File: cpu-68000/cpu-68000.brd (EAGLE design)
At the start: 149.9 x 99.7 mm, 101 parts, among them IC201 AS6C4008, IC202 AS6C4008, IC203 39SF040, IC204 39SF040, IC301 XR68C681, IC302 DS1244Y, IC303 MAX232, IC401 GAL22V10, IC402 GAL22V10, IC403 74HC14D, IC404 LM3724, IC405 74HC175D, J201 POWER_JACK, Q301 3.6864 MHz

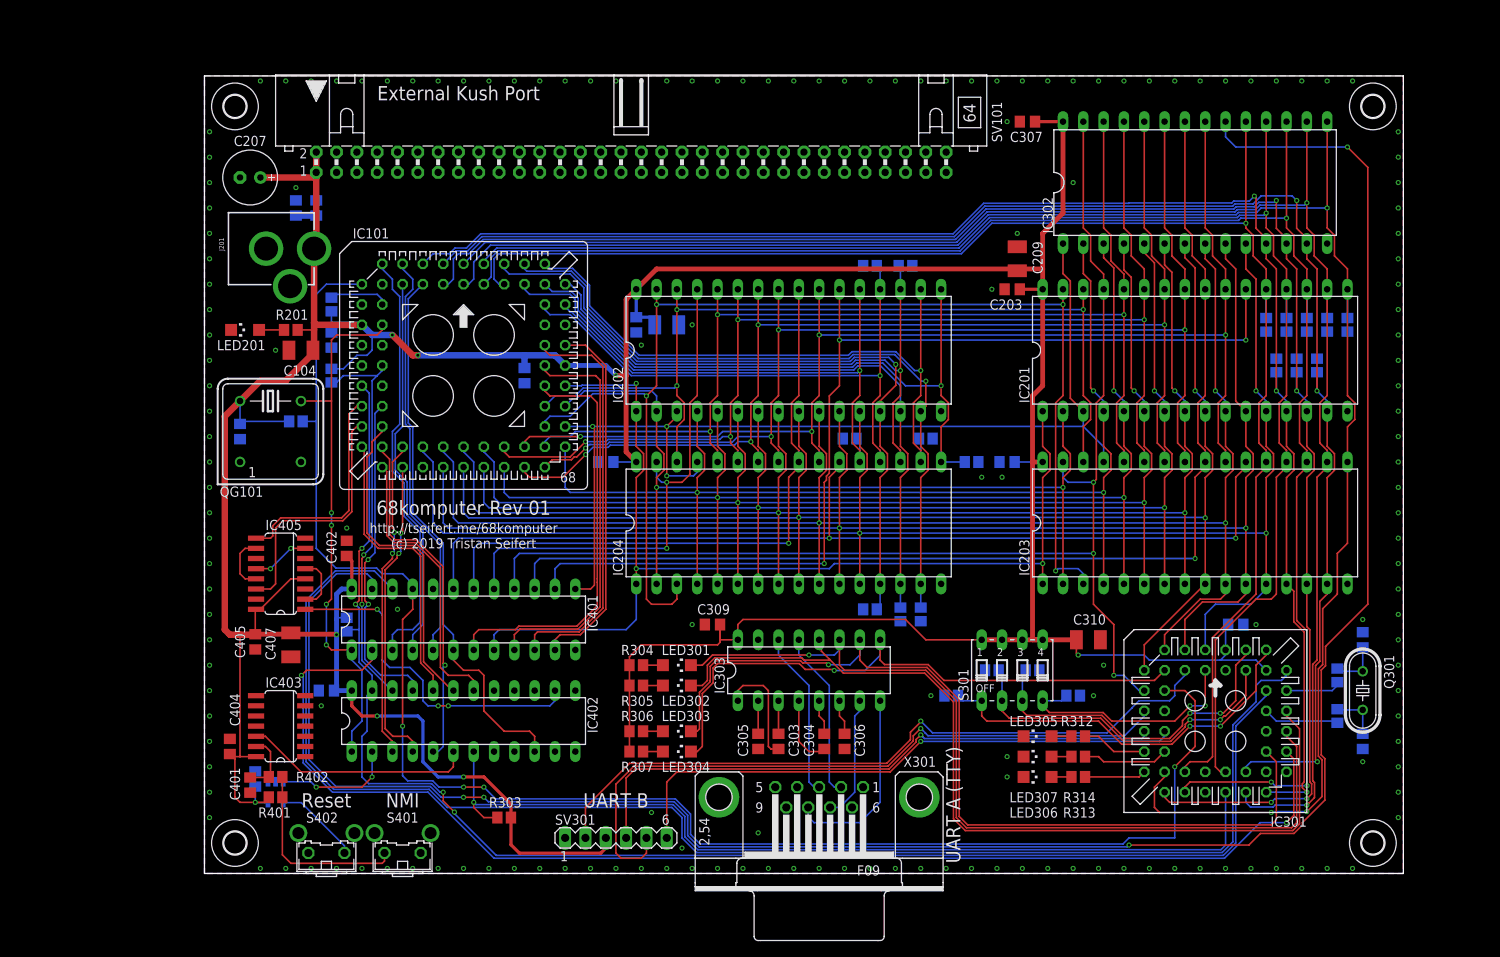
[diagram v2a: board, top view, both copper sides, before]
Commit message: Finished routing expansion connector for 68000 board
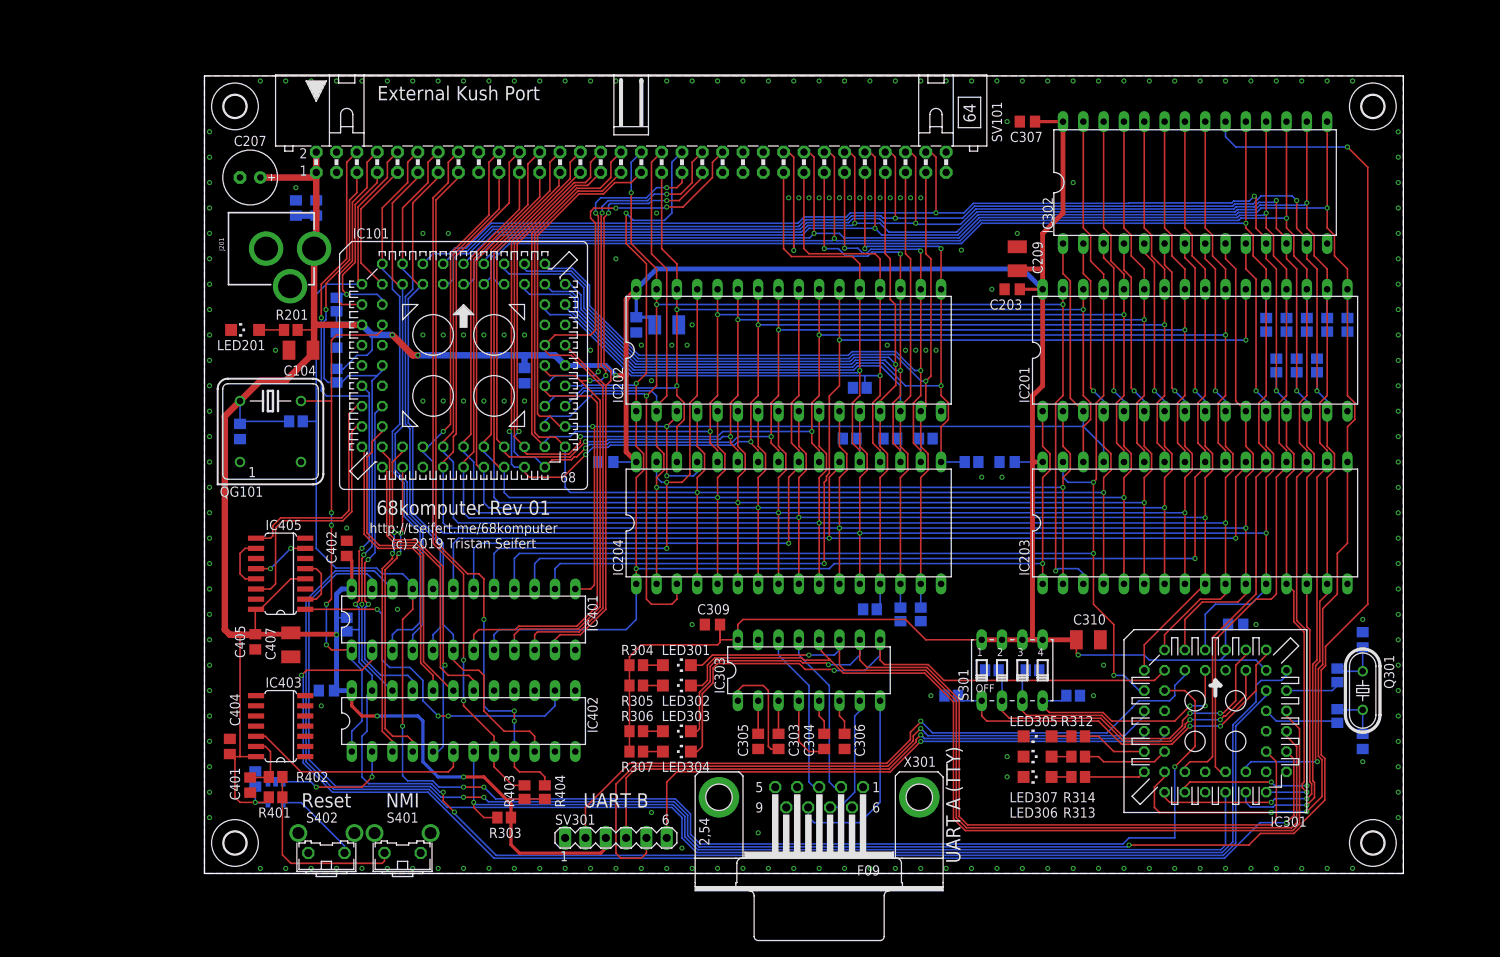
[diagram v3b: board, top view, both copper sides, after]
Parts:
- removed R6, R7: 10k, rcl:R2012
- added R118, R119, R403, R404: 10k, rcl:R2012
- moved C102 0.64 mm to (16.5, 66.7)
- moved R103 0.64 mm to (16.5, 62.2)
- moved R104 0.64 mm to (16.5, 71.1)
- renumbered R1 to R113, R2 to R114, R3 to R115, R4 to R116, R5 to R117, R8 to R120
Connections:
- net !AS: now also SV101.13
- net !BG: now also SV101.9
- net !BGACK: now also SV101.8
- net !BR: now also SV101.7
- net !DTACK: now also SV101.10
- net !EXTI_A: now also R403.1, SV101.16
- net !EXTI_B: now also R404.1, SV101.15
- net !HALT: now also SV101.5
- net !LDS: now also SV101.11
- net !RESET: now also SV101.6
- net !UDS: now also SV101.14
- net +5V: now also R403.2, R404.2
- net A1: now also SV101.20
- net A10: now also SV101.27
- net A11: now also SV101.30
- net A12: now also SV101.29
- net A13: now also SV101.31
- net A14: now also SV101.32
- net A15: now also SV101.33
- net A16: now also SV101.34
- net A17: now also SV101.36
- net A18: now also SV101.35
- net A19: now also SV101.38
- net A2: now also SV101.22
- net A20: now also SV101.37
- net A21: now also SV101.40
- net A22: now also SV101.39
- net A23: now also SV101.42
- net A3: now also SV101.19
- net A4: now also SV101.24
- net A5: now also SV101.21
- net A6: now also SV101.23
- net A7: now also SV101.26
- net A8: now also SV101.25
- net A9: now also SV101.28
- net D0: now also SV101.62
- net D1: now also SV101.60
- net D10: now also SV101.61
- net D11: now also SV101.55
- net D12: now also SV101.53
- net D13: now also R118.2, SV101.51; no longer R6.2
- net D14: now also R119.2, SV101.49; no longer R7.2
- net D15: now also SV101.47
- net D2: now also SV101.58
- net D3: now also SV101.56
- net D4: now also SV101.54
- net D5: now also SV101.52
- net D6: now also SV101.50
- net D7: now also SV101.48
- net D8: now also SV101.57
- net D9: now also SV101.59
- net GND: now also R118.1, R119.1, SV101.17, SV101.18, SV101.45, SV101.46, X301.G1, X301.G2; no longer R6.1, R7.1
- net R/!W!: now also SV101.12
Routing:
- net !EXTI_B: track 0.00 -> 87.6 mm, vias 0 -> 3
- net !EXTI_A: track 0.00 -> 86.1 mm, vias 0 -> 2
- net A12: track 147.4 -> 192.5 mm, vias 4 -> 5
- net A11: track 154.6 -> 198.4 mm
- net A14: track 139.3 -> 183.2 mm
- net A13: track 139.4 -> 182.7 mm
- net A4: track 179.4 -> 222.7 mm
- net A2: track 188.3 -> 231.6 mm
- net A15: track 130.6 -> 173.2 mm
- net A10: track 148.5 -> 190.6 mm, vias 4 -> 5
- net A20: track 52.0 -> 93.8 mm, vias 0 -> 3
- net A9: track 147.7 -> 189.3 mm
- net A23: track 50.8 -> 92.1 mm, vias 0 -> 2
- net A8: track 147.6 -> 188.8 mm
- net A1: track 195.4 -> 236.6 mm, vias 3 -> 4
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
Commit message: Enlarged 68000 board to 100x160mm (Eurocard size) Moved high/low words sections to accomodate ZIF sockets better
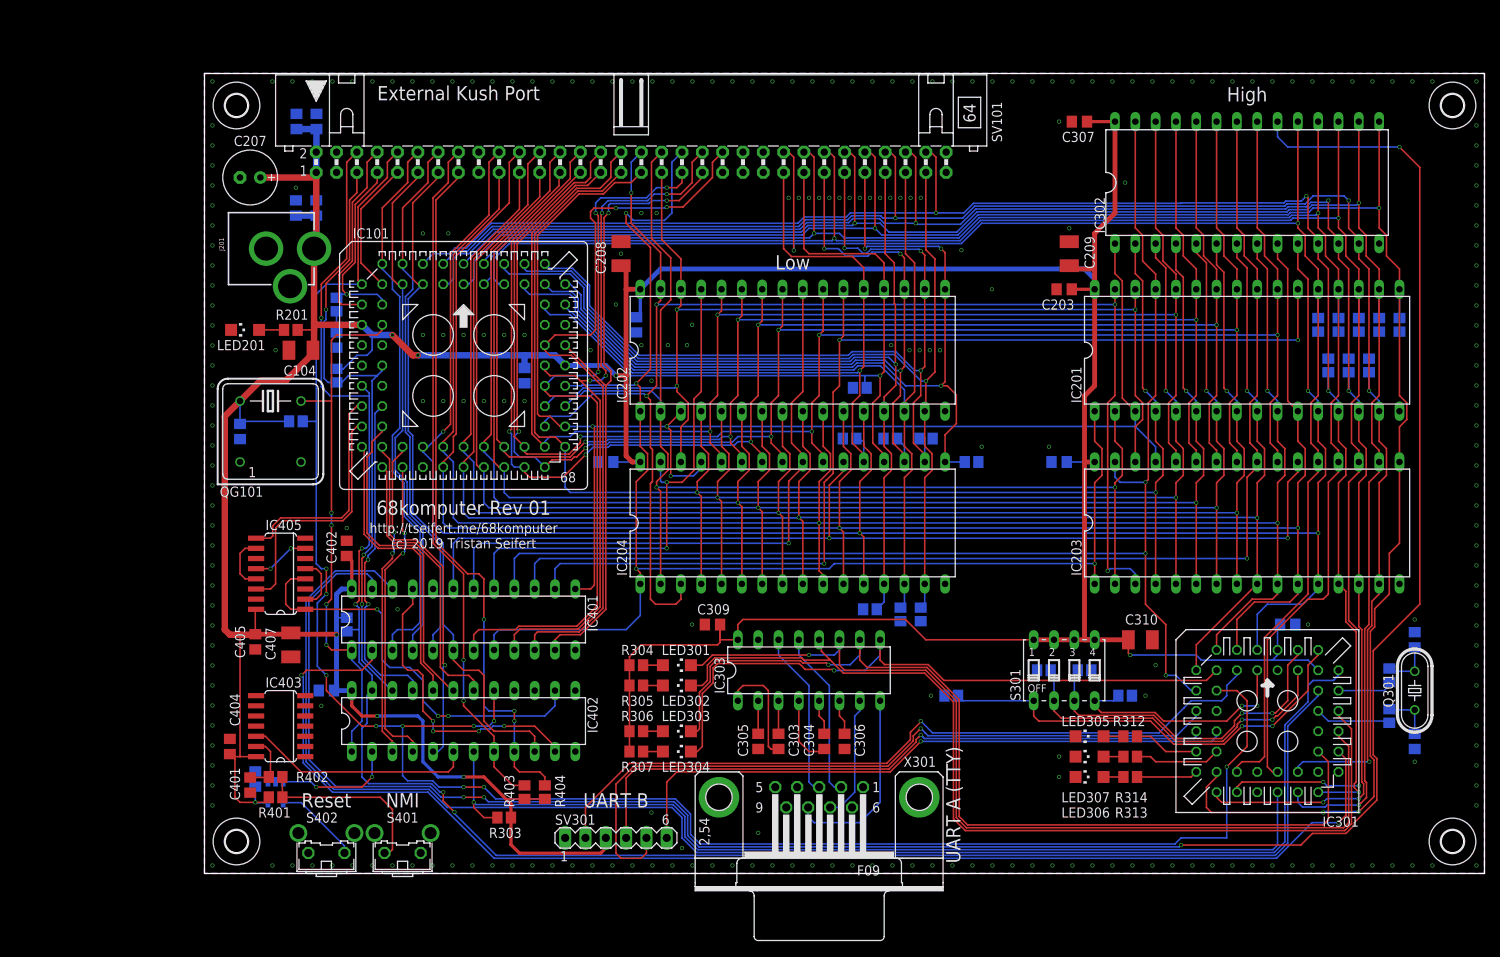
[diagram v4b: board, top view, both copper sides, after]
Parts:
- added C1: 1µF, rcl:C0805
- added C105: 100nF, rcl:C0805
- moved C208 10.6 mm to (52.1, 77.5), flipped to the top, turned to 90 degrees
- moved H104 9.95 mm to (156.0, 4.00)
- moved H103 9.95 mm to (156.0, 96.0)
- moved C209 6.53 mm to (108.1, 77.5)
- moved IC301 6.50 mm to (132.9, 19.1)
- moved C203 6.50 mm to (107.5, 73.0)
- moved C206 6.50 mm to (106.8, 51.4)
- moved C301 6.50 mm to (151.3, 16.5)
- moved C302 6.50 mm to (151.3, 29.2)
- moved C307 6.50 mm to (109.4, 94.0)
- moved C308 6.50 mm to (135.4, 31.1)
- moved C310 6.50 mm to (117.0, 29.2)
- moved LED305 6.50 mm to (110.6, 17.1)
- moved LED306 6.50 mm to (110.6, 12.1)
- moved LED307 6.50 mm to (110.6, 14.6)
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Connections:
- removed net N$22: IC402.11
- removed net N$23: IC402.13
- new net !ADDR_GOOD: IC401.21, IC402.11
- net !BERR_TIMER_CLR: now also IC405.4
- net !DTACK: now also IC402.17; no longer IC401.21
- net +5V: now also C1.1, C105.1; no longer IC405.4
- net GND: now also C1.2, C105.2, SV101.41, SV101.43, SV101.44
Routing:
- net !ADDR_GOOD: track 0.00 -> 37.8 mm, vias 0 -> 4
- net !DTACK: track 221.2 -> 242.0 mm, vias 4 -> 10
- net +5V: track 556.8 -> 570.5 mm
- net !BERR_TIMER_CLR: track 44.0 -> 51.9 mm
- net A19: track 170.7 -> 178.4 mm
- net A16: track 170.9 -> 178.2 mm
- net A17: track 144.1 -> 151.4 mm
- net A18: track 128.5 -> 135.6 mm
- net A2: track 231.6 -> 238.5 mm
- net A9: track 189.3 -> 196.2 mm
- net A5: track 201.2 -> 208.1 mm
- net A10: track 190.6 -> 197.5 mm
- net A8: track 188.8 -> 195.7 mm
- net A7: track 195.9 -> 202.8 mm
- net A6: track 197.4 -> 204.3 mm
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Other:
- board size 149.9 x 99.7 mm -> 160 x 100 mm
- board text added: "High"
- board text added: "Low"

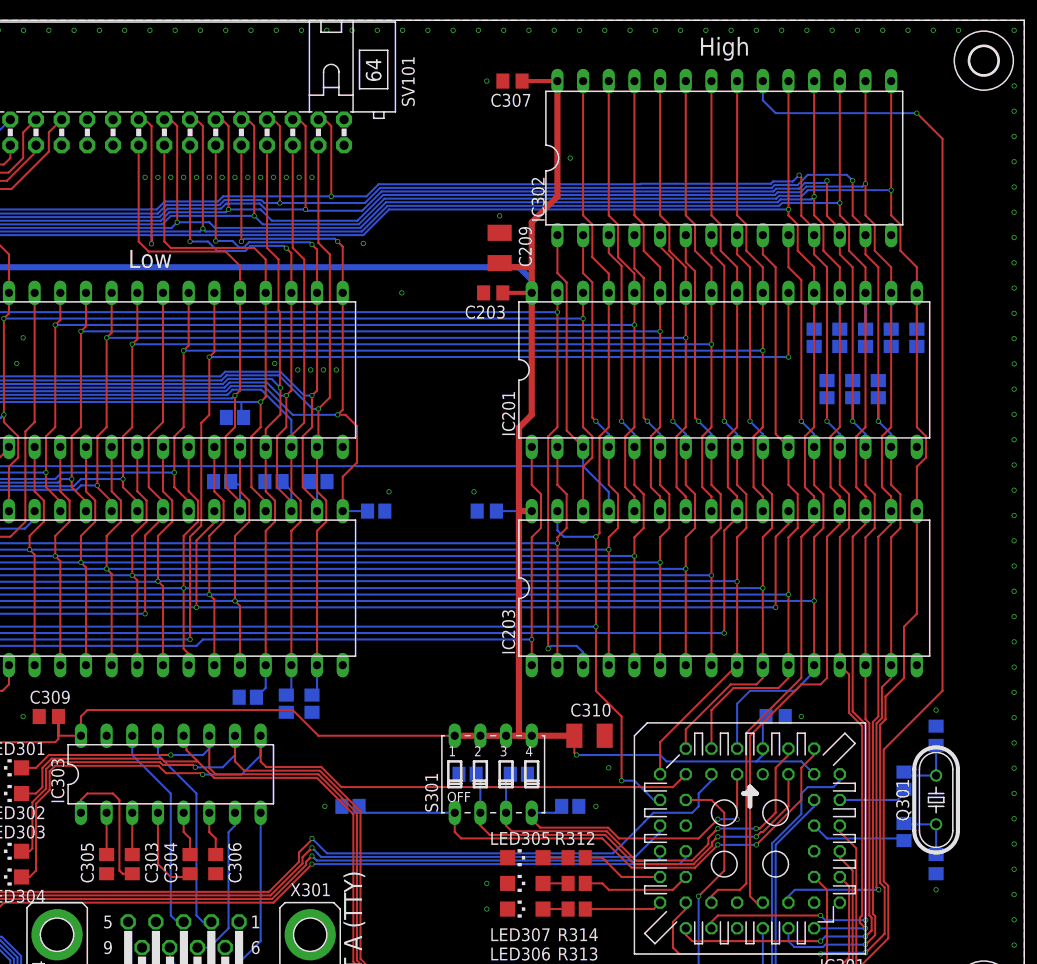
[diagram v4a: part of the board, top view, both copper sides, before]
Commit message: CPU board: 	- Clean up some traces
IO board:
	- Started work on super IO board
	- UARTs, parallel port, PS/2 keyboard/mouse interface, I2C

2MB RAM Expansion:
	- Added some address decoding
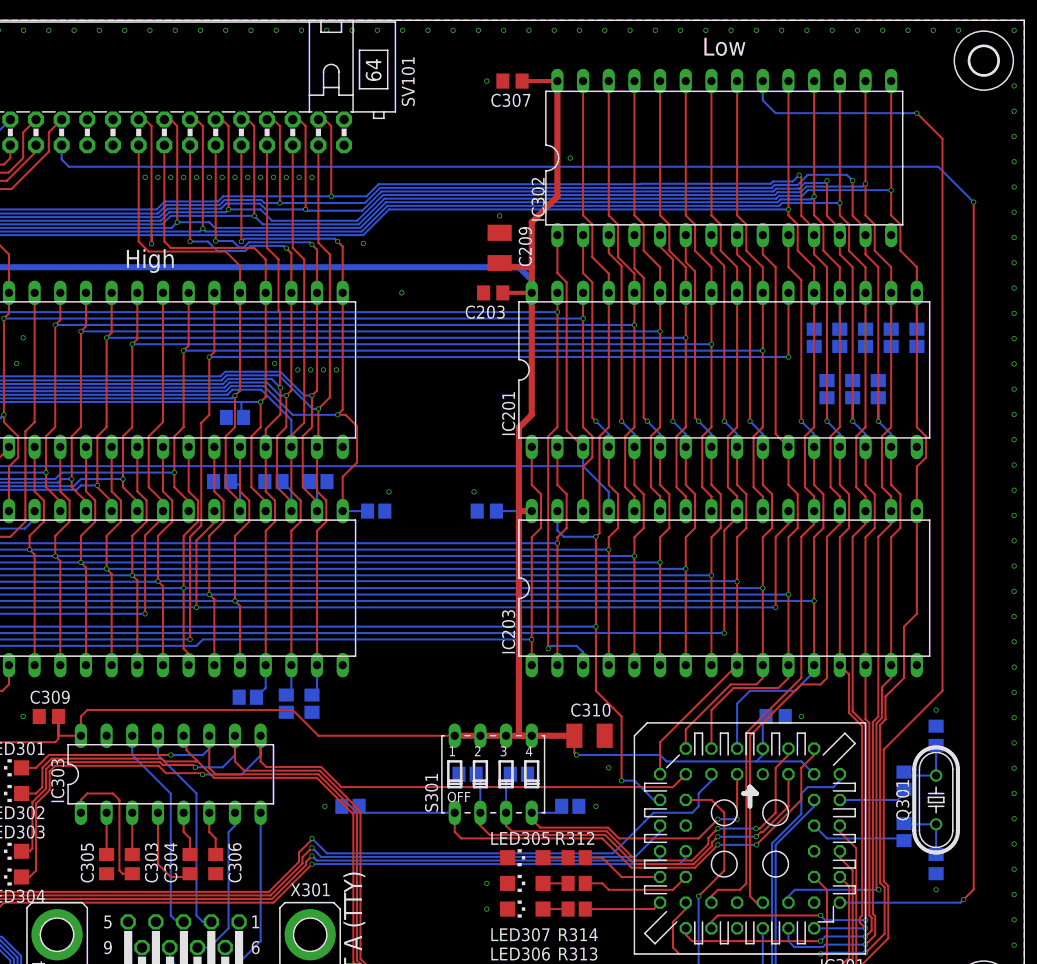
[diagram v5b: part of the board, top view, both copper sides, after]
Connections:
- new net !EXT_ID: IC301.29, SV101.41
- net GND: no longer SV101.41
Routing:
- net !EXT_ID: track 0.00 -> 175.2 mm, vias 0 -> 2
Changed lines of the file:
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@@
 <?xml version="1.0" encoding="utf-8"?>
 <!DOCTYPE eagle SYSTEM "eagle.dtd">
-<eagle version="9.4.2">
+<eagle version="9.5.2">
 <drawing>
 <settings>
@@
 <text x="21.59" y="98.425" size="1.778" layer="25" align="top-left">External Kush Port</text>
 <text x="24.765" y="8.255" size="1.778" layer="25" rot="R180" align="top-center">NMI</text>
-<text x="73.525" y="75.5" size="1.778" layer="25" align="bottom-center">Low</text>
-<text x="130.325" y="96.5" size="1.778" layer="25" align="bottom-center">High</text>
+<text x="73.525" y="75.5" size="1.778" layer="25" align="bottom-center">High</text>
+<text x="130.325" y="96.5" size="1.778" layer="25" align="bottom-center">Low</text>
 </plain>
 <attributes>
@@
 <contactref element="C105" pad="2"/>
 <contactref element="C1" pad="2"/>
-<contactref element="SV101" pad="41"/>
 <contactref element="SV101" pad="43"/>
 <contactref element="SV101" pad="44"/>
@@
 <wire x1="41.275" y1="18.415" x2="43.815" y2="15.875" width="0.2032" layer="1"/>
 </signal>
+<signal name="!EXT_ID">
+<contactref element="SV101" pad="41"/>
+<contactref element="IC301" pad="29"/>
+<wire x1="141.755" y1="12.7" x2="153.7" y2="12.7" width="0.2032" layer="16"/>
+<wire x1="153.7" y1="12.7" x2="154" y2="13" width="0.2032" layer="16"/>
+<via x="154" y="13" extent="1-16" drill="0.35"/>
+<wire x1="155" y1="82" x2="155" y2="14" width="0.2032" layer="1"/>
+<wire x1="154" y1="13" x2="155" y2="14" width="0.2032" layer="1"/>
+<wire x1="64.77" y1="87.63" x2="64.77" y2="86.23" width="0.2032" layer="16"/>
+<wire x1="64.77" y1="86.23" x2="65.5" y2="85.5" width="0.2032" layer="16"/>
+<wire x1="151.5" y1="85.5" x2="155" y2="82" width="0.2032" layer="16"/>
+<via x="155" y="82" extent="1-16" drill="0.35"/>
+<wire x1="151.5" y1="85.5" x2="65.5" y2="85.5" width="0.2032" layer="16"/>
+</signal>
 </signals>
